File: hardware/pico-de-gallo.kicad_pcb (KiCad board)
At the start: 4 copper layers, 50 x 69.5 mm, 14 parts, among them J1 Conn_02x08_Odd_Even, J2 Conn_01x02, J3 Conn_01x04, J4 Conn_01x05, J5 Conn_01x02, J6 Conn_01x03, J7 Conn_02x05_Odd_Even

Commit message: Minor updates
Signed-off-by: Felipe Balbi <febalbi@microsoft.com>
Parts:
- moved A1 135.0 mm to (152.1, 72.0)
- moved H1 135.0 mm to (132.6, 51.5)
- moved H2 135.0 mm to (172.6, 51.5)
- moved H3 135.0 mm to (132.6, 110.5)
- moved H4 135.0 mm to (172.6, 110.5)
- moved J1 135.0 mm to (129.6, 79.5)
- moved J2 135.0 mm to (129.6, 102.5)
- moved J3 135.0 mm to (140.0, 104.5)
- moved J4 135.0 mm to (155.1, 104.5)
- moved J5 135.0 mm to (129.6, 60.0)
- moved J6 135.0 mm to (129.6, 68.5)
- moved J7 135.0 mm to (171.4, 90.6)
- moved REF** 135.0 mm to (172.9, 81.8)
- moved REF** 135.0 mm to (170.1, 96.5)

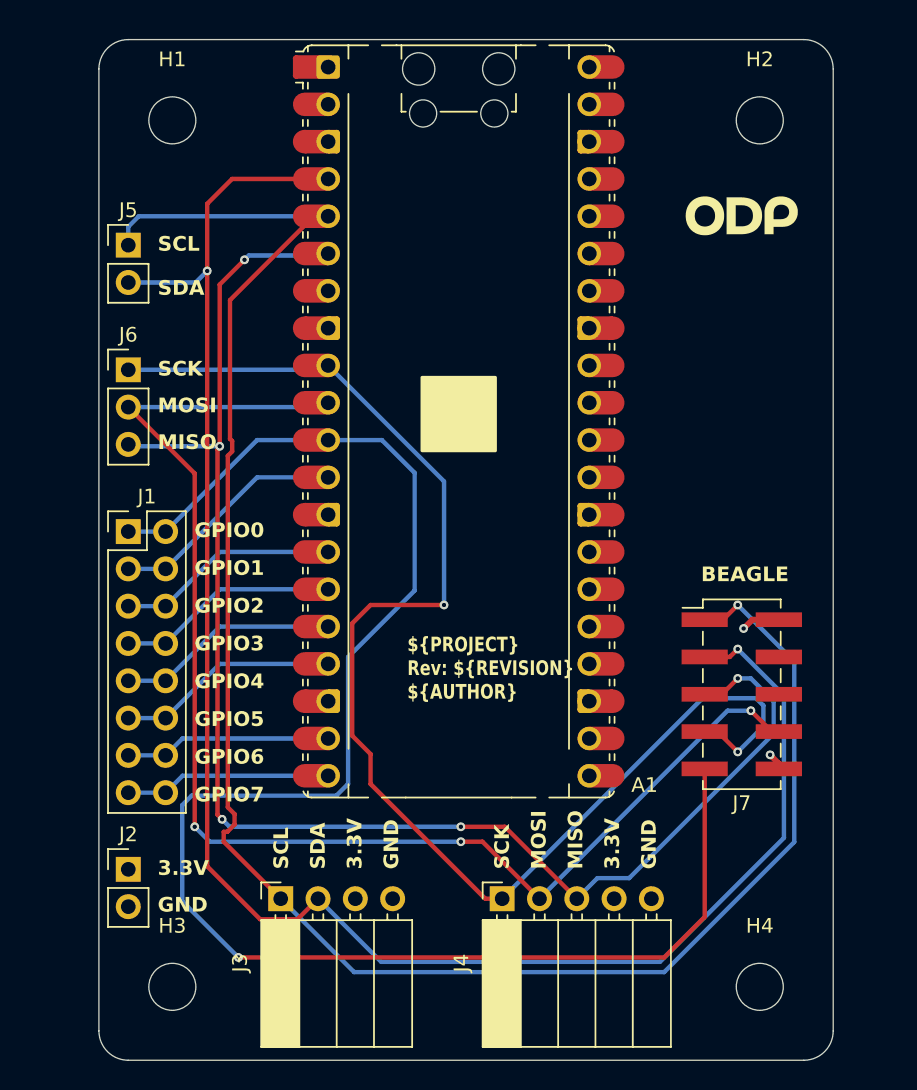
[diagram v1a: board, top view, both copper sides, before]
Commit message: Pico de Gallo Hardware v1.1
Update the PCB for revision 1.1 of the main board.
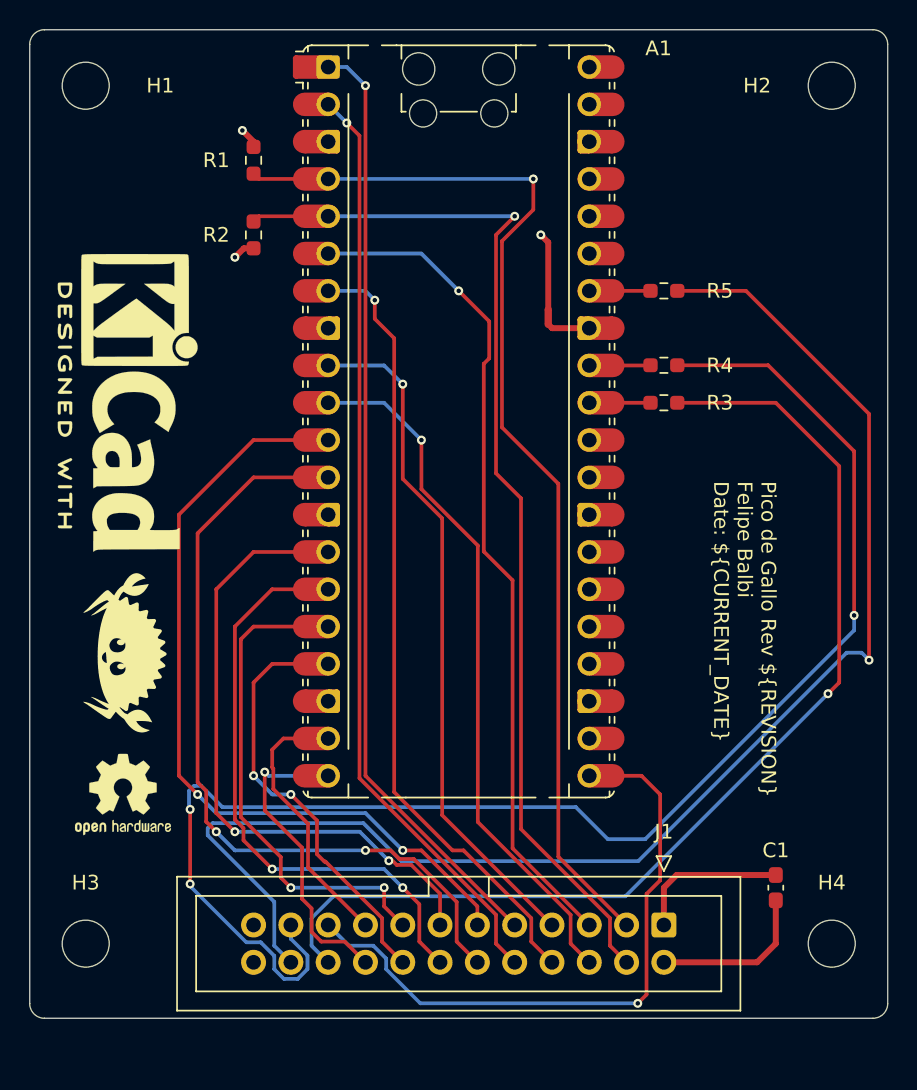
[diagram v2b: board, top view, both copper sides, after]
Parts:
- removed J2, J5: Conn_01x02, Connector_PinHeader_2.54mm:PinHeader_1x02_P2.54mm_Vertical
- removed J3: Conn_01x04, Connector_PinSocket_2.54mm:PinSocket_1x04_P2.54mm_Horizontal
- removed J4: Conn_01x05, Connector_PinSocket_2.54mm:PinSocket_1x05_P2.54mm_Horizontal
- removed J6: Conn_01x03, Connector_PinHeader_2.54mm:PinHeader_1x03_P2.54mm_Vertical
- removed J7: Conn_02x05_Odd_Even, Connector_PinHeader_2.54mm:PinHeader_2x05_P2.54mm_Vertical_SMD
- added C1: 100nF, Capacitor_SMD:C_0603_1608Metric_Pad1.08x0.95mm_HandSolder, F.Cu at (173.7, 103.8)
- added NT1: NetTie_2, NetTie:NetTie-2_SMD_Pad0.5mm, F.Cu at (158.2, 64.9)
- added R1: 4.7k, Resistor_SMD:R_0603_1608Metric_Pad0.98x0.95mm_HandSolder, F.Cu at (138.1, 54.3)
- added R2: 4.7k, Resistor_SMD:R_0603_1608Metric_Pad0.98x0.95mm_HandSolder, F.Cu at (138.1, 59.3)
- added R3: 100, Resistor_SMD:R_0603_1608Metric_Pad0.98x0.95mm_HandSolder, F.Cu at (166.1, 70.8)
- added R4: 100, Resistor_SMD:R_0603_1608Metric_Pad0.98x0.95mm_HandSolder, F.Cu at (166.1, 68.2)
- added R5: 100, Resistor_SMD:R_0603_1608Metric_Pad0.98x0.95mm_HandSolder, F.Cu at (166.1, 63.1)
- J1: value Conn_02x08_Odd_Even -> Conn_02x12_Odd_Even; footprint Connector_PinHeader_2.54mm:PinHeader_2x08_P2.54mm_Vertical -> Connector_IDC:IDC-Header_2x12_P2.54mm_Vertical
- REF** (x2): moved to F.Cu
- moved REF** 43.9 mm to (130.4, 70.8), turned to -90 degrees
- moved REF** 40.9 mm to (129.2, 97.4), turned to 0 degrees
- moved J1 36.0 mm to (152.1, 107.6), turned to -90 degrees
- moved H3 6.59 mm to (126.7, 107.6)
- moved H1 6.35 mm to (126.7, 49.2)
- moved H4 5.71 mm to (177.5, 107.6)
- moved H2 5.44 mm to (177.5, 49.2)
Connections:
- A1 pad 1: unconnected-(A1-GPIO0-Pad1) -> /UART_TX
- A1 pad 10: /MOSI -> /SPI_MOSI
- A1 pad 16: /GPIO4 -> /PWM0
- A1 pad 17: /GPIO5 -> /PWM1
- A1 pad 19: /GPIO6 -> /PWM2
- A1 pad 2: unconnected-(A1-GPIO1-Pad2) -> /UART_RX
- A1 pad 20: /GPIO7 -> /PWM3
- A1 pad 21: unconnected-(A1-GPIO16-Pad21) -> /ONEWIRE
- A1 pad 31: unconnected-(A1-GPIO26_ADC0-Pad31)_1 -> /ADC0
- A1 pad 32: unconnected-(A1-GPIO27_ADC1-Pad32) -> /ADC1
- A1 pad 33: unconnected-(A1-AGND-Pad33)_1 -> Net-(A1-AGND)
- A1 pad 34: unconnected-(A1-GPIO28_ADC2-Pad34) -> /ADC2
- A1 pad 35: unconnected-(A1-ADC_VREF-Pad35) -> +3V3
- A1 pad 4: /SDA -> /I2C_SDA
- A1 pad 5: /SCL -> /I2C_SCL
- A1 pad 6: /MISO -> /SPI_MISO
- A1 pad 7: unconnected-(A1-GPIO5-Pad7) -> /SPI_CS
- A1 pad 9: /CLK -> /SPI_SCK
- J1 pad 1: /GPIO0 -> +3V3
- J1 pad 10: /GPIO4 -> /UART_RX
- J1 pad 11: /GPIO5 -> /GPIO0
- J1 pad 12: /GPIO5 -> /GPIO1
- J1 pad 13: /GPIO6 -> /GPIO2
- J1 pad 14: /GPIO6 -> /GPIO3
- J1 pad 15: /GPIO7 -> /PWM0
- J1 pad 16: /GPIO7 -> /PWM1
- J1 pad 2: /GPIO0 -> GND
- J1 pad 3: /GPIO1 -> /I2C_SDA
- J1 pad 4: /GPIO1 -> /I2C_SCL
- J1 pad 5: /GPIO2 -> /SPI_MISO
- J1 pad 6: /GPIO2 -> /SPI_MOSI
- J1 pad 7: /GPIO3 -> /SPI_SCK
- J1 pad 8: /GPIO3 -> /SPI_CS
- J1 pad 9: /GPIO4 -> /UART_TX
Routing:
- net /SCL: track 128.5 -> 0.00 mm, vias 1 -> 0
- net /SDA: track 123.0 -> 0.00 mm, vias 2 -> 0
- net /MISO: track 103.6 -> 0.00 mm, vias 5 -> 0
- net /ADC1_R: track 0.00 -> 100.9 mm, vias 0 -> 3
- net /ADC2_R: track 0.00 -> 97.1 mm, vias 0 -> 1
- net /CLK: track 94.1 -> 0.00 mm, vias 2 -> 0
- net /MOSI: track 91.9 -> 0.00 mm, vias 3 -> 0
- net /I2C_SDA: track 0.00 -> 73.6 mm, vias 0 -> 1
- net /ADC0_R: track 0.00 -> 73.6 mm, vias 0 -> 1
- net /I2C_SCL: track 0.00 -> 72.1 mm, vias 0 -> 1
- net /UART_TX: track 0.00 -> 64.4 mm, vias 0 -> 1
- net /UART_RX: track 0.00 -> 63.7 mm, vias 0 -> 1
- net /GPIO0: track 112.9 -> 55.3 mm, vias 1 -> 2
- net /SPI_MISO: track 0.00 -> 57.1 mm, vias 0 -> 1
- net /SPI_CS: track 0.00 -> 54.0 mm, vias 0 -> 1
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- added copper zone on In1.Cu, net +3V3
- added copper zone on In2.Cu, net GND
- removed copper zone on In2.Cu, net +3V3
- removed copper zone on In1.Cu, net GND
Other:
- board size 50 x 69.5 mm -> 58.4 x 67.3 mm
- board text added: "Pico de Gallo Rev ${REVISION} Felipe Balbi Date: ${CURRENT_DATE}"
- board text removed: "${PROJECT} Rev: ${REVISION} ${AUTHOR}"
- board text removed: "3.3V"
- board text removed: "BEAGLE"
- board text removed: "GND"
- board text removed: "GPIO0"
- board text removed: "GPIO1"
- board text removed: "GPIO2"
- board text removed: "GPIO3"
- board text removed: "GPIO4"
- board text removed: "GPIO5"
- board text removed: "GPIO6"
- board text removed: "GPIO7"
- board text removed: "MISO"
- board text removed: "MOSI"
- board text removed: "SCK"
- board text removed: "SCL"
- board text removed: "SDA"
